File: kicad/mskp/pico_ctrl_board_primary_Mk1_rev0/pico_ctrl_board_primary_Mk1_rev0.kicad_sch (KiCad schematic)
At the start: 9 parts, among them J4 USB_C_Receptacle_USB2.0, J5 Conn_01x04_Socket, J8 Conn_01x12_Socket, J9 Conn_01x03_Socket, SW3 SW_Omron_B3FS, U1 Raspberry_Pi_Pico

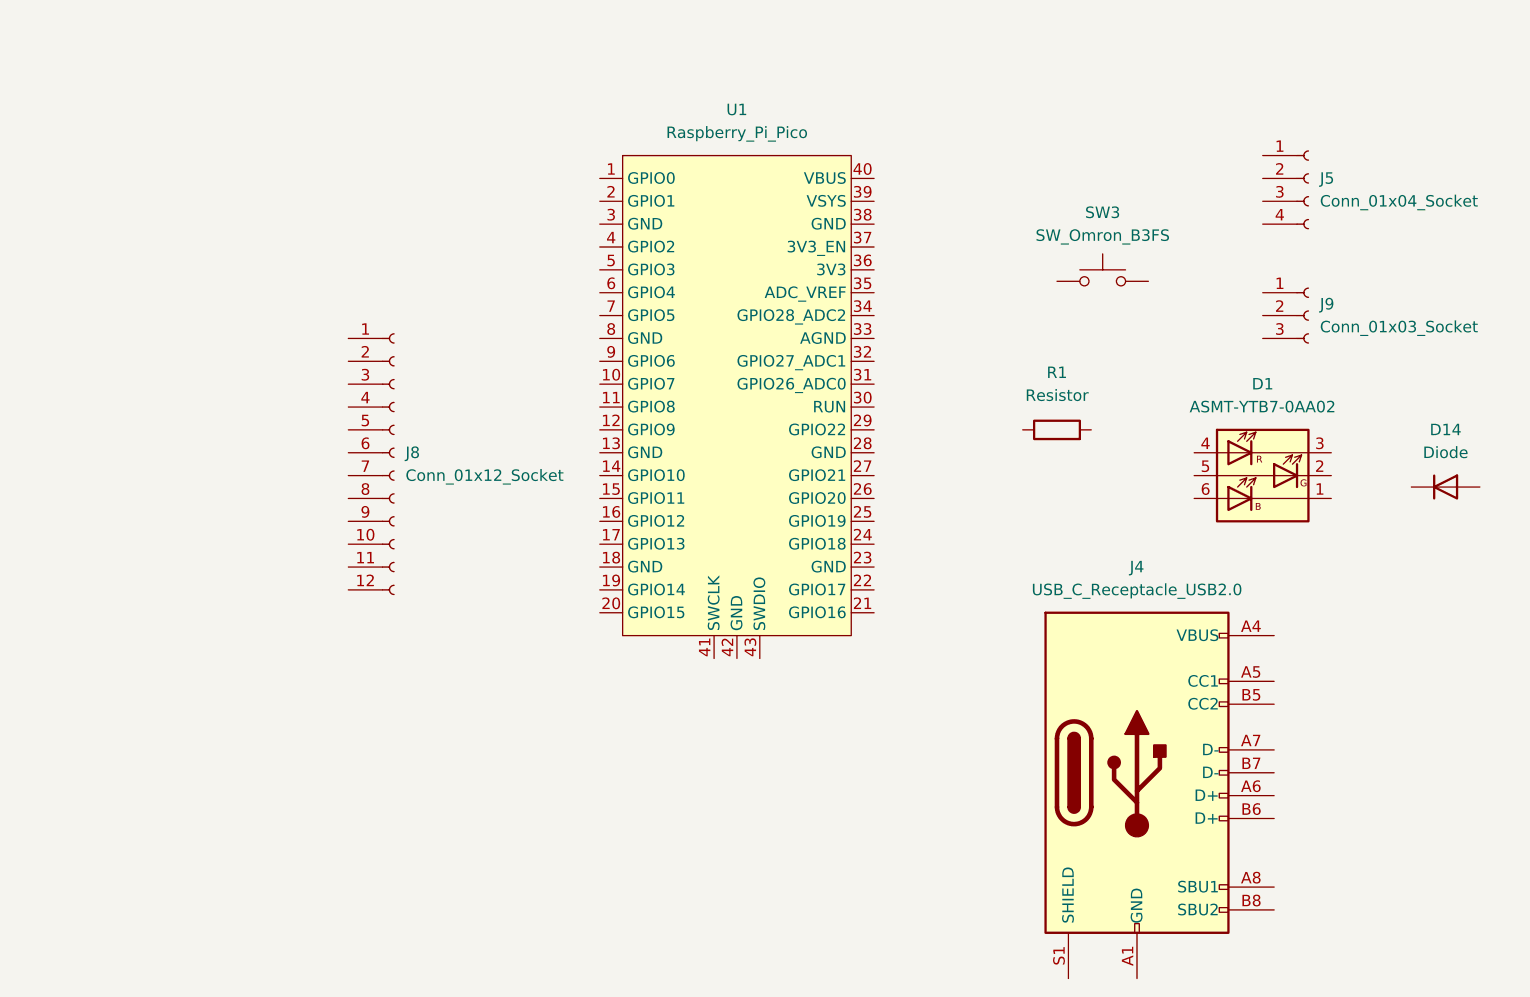
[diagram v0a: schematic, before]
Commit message: Removes the mksp_Mk1_rev0 project in favor of board-specific projects
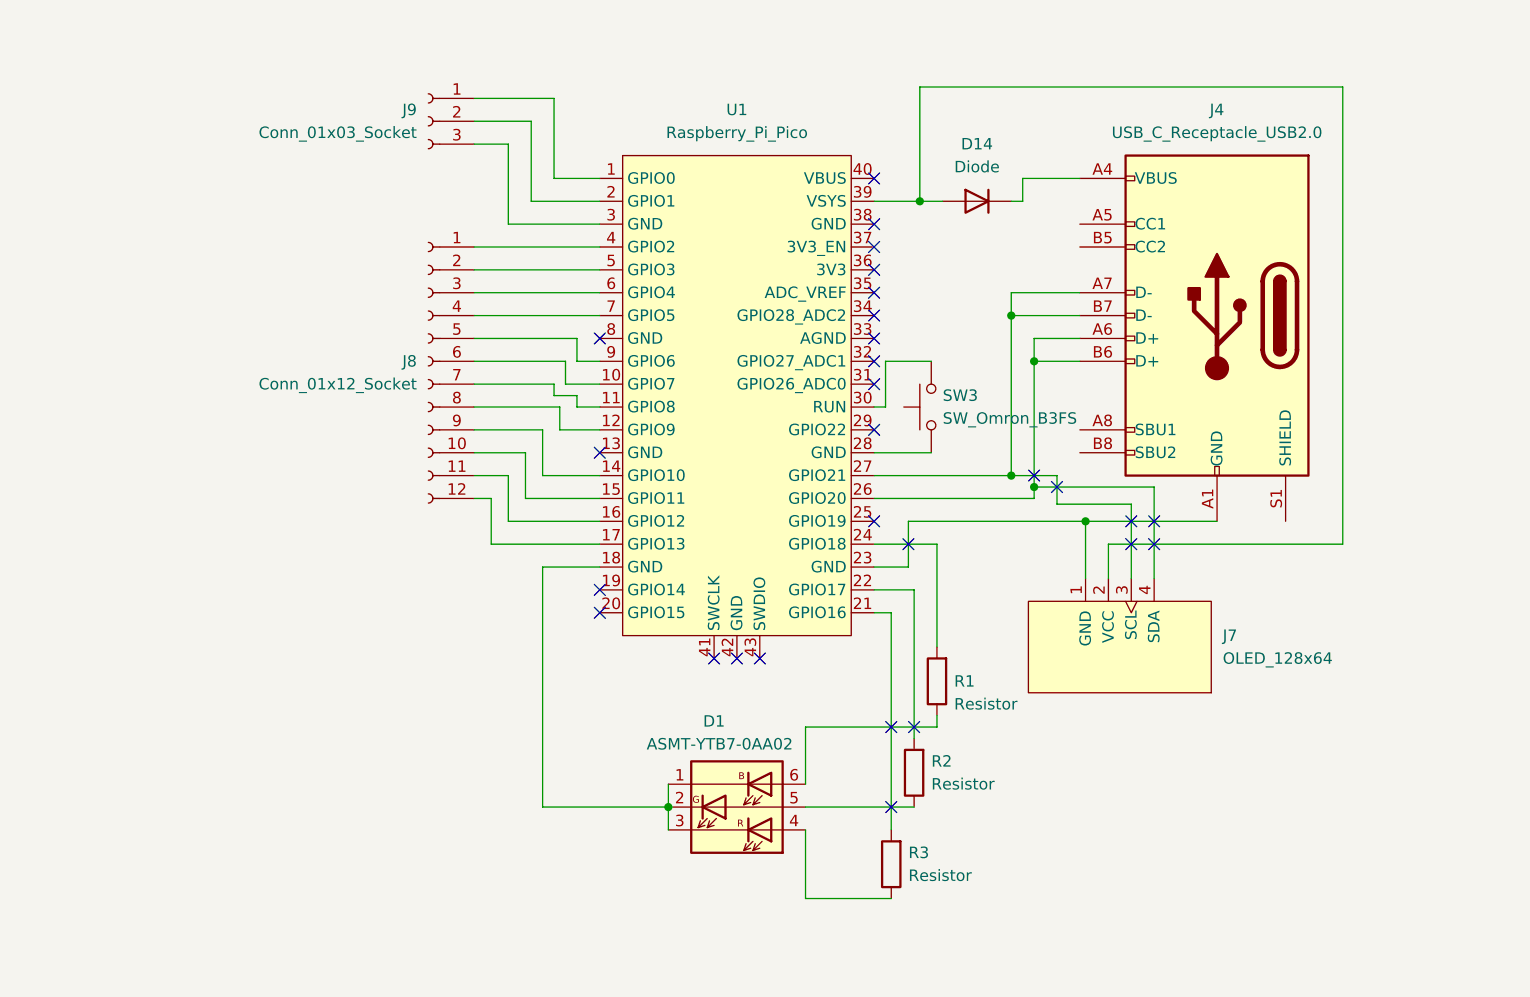
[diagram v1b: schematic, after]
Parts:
- removed J5: Conn_01x04_Socket, symbol Connector:Conn_01x04_Socket
- added J7: OLED_128x64, ScottoKeebs_Components:OLED_128x64, symbol ScottoKeebs:OLED_128x64
- added R2, R3: Resistor, symbol ScottoKeebs:Placeholder_Resistor
- D14: footprint (none) -> ScottoKeebs_Components:Diode_DO-35
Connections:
- net at U1.1 (GPIO0): now also J9.1 (Pin_1)
- net at U1.10 (GPIO7): now also J8.6 (Pin_6)
- net at U1.11 (GPIO8): now also J8.7 (Pin_7)
- net at U1.12 (GPIO9): now also J8.8 (Pin_8)
- net at U1.14 (GPIO10): now also J8.9 (Pin_9)
- net at U1.15 (GPIO11): now also J8.10 (Pin_10)
- net at U1.16 (GPIO12): now also J8.11 (Pin_11)
- net at U1.17 (GPIO13): now also J8.12 (Pin_12)
- net at U1.18 (GND): now also D1.1 (KB), D1.2 (KG), D1.3 (KR)
- net at U1.2 (GPIO1): now also J9.2 (Pin_2)
- net at U1.21 (GPIO16): now also R3.2
- net at U1.22 (GPIO17): now also R2.2
- net at U1.23 (GND): now also J4.A1 (GND), J4.A12 (GND), J4.B1 (GND), J4.B12 (GND), J7.1 (GND)
- net at U1.24 (GPIO18): now also R1.2
- net at U1.26 (GPIO20): now also J4.A6 (D+), J4.B6 (D+), J7.4 (SDA)
- net at U1.27 (GPIO21): now also J4.A7 (D-), J4.B7 (D-), J7.3 (SCL)
- net at U1.28 (GND): now also SW3.1
- net at U1.3 (GND): now also J9.3 (Pin_3)
- net at U1.30 (RUN): now also SW3.2
- net at U1.39 (VSYS): now also D14.2 (A), J7.2 (VCC)
- net at U1.4 (GPIO2): now also J8.1 (Pin_1)
- net at U1.5 (GPIO3): now also J8.2 (Pin_2)
- net at U1.6 (GPIO4): now also J8.3 (Pin_3)
- net at U1.7 (GPIO5): now also J8.4 (Pin_4)
- net at U1.9 (GPIO6): now also J8.5 (Pin_5)
- net at D14.1 (K): now also J4.A4 (VBUS), J4.A9 (VBUS), J4.B4 (VBUS), J4.B9 (VBUS)
- net at D1.4 (AR): now also R3.1
- net at D1.5 (AG): now also R2.1
- net at D1.6 (AB): now also R1.1
- no-connect marks 0 -> 28
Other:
- moved on the sheet: D1, D14, J4, J8, J9, R1, SW3

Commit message: Initial work on pico_ctrl_board_primary_Mk1_rev0 layout
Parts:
- added J1: Conn_01x06_Socket, symbol Connector:Conn_01x06_Socket
- J4: footprint (none) -> Connector_USB:USB_C_Receptacle_GCT_USB4110
- J8: footprint (none) -> Connector_JST:JST_GH_SM12B-GHS-TB_1x12-1MP_P1.25mm_Horizontal
- J9: footprint (none) -> Connector_JST:JST_SH_SM03B-SRSS-TB_1x03-1MP_P1.00mm_Horizontal
- R1, R2, R3: footprint (none) -> Resistor_THT:R_Axial_DIN0204_L3.6mm_D1.6mm_P5.08mm_Horizontal
- SW3: footprint (none) -> Button_Switch_SMD:SW_SPST_Omron_B3FS-101xP
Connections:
- net GND: now reaches U1.38 (GND)
- net +5V: now reaches U1.40 (VBUS)
- no-connect marks 28 -> 33
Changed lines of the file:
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@@
   (junction (at 151.13 123.19) (diameter 0) (color 0 0 0 0)
   )
-  (no_connect (at 173.99 58.42))
+  (no_connect (at 196.85 81.28))
   (no_connect (at 143.51 99.06))
   (no_connect (at 178.435 114.3))
@@
   (no_connect (at 173.99 63.5))
   (no_connect (at 175.895 114.3))
+  (no_connect (at 173.99 45.085))
   (no_connect (at 173.99 66.04))
+  (no_connect (at 196.85 83.82))
   (no_connect (at 173.99 76.2))
   (no_connect (at 143.51 71.12))
   (no_connect (at 177.8 93.98))
   (no_connect (at 202.565 93.98))
-  (no_connect (at 173.99 53.34))
   (no_connect (at 173.99 73.66))
   (no_connect (at 191.77 86.36))
@@
   (no_connect (at 173.99 68.58))
   (no_connect (at 175.895 123.19))
+  (no_connect (at 196.85 58.42))
   (no_connect (at 173.99 91.44))
   (no_connect (at 173.99 60.96))
   (no_connect (at 173.99 81.28))
+  (no_connect (at 196.85 60.96))
   (no_connect (at 202.565 91.44))
   (no_connect (at 143.51 101.6))
   (no_connect (at 161.29 106.68))
+  (no_connect (at 176.53 55.88))
+  (no_connect (at 219.71 91.44))
   (no_connect (at 205.105 93.98))
   (no_connect (at 173.99 71.12))
@@
     (stroke (width 0) (type default))
   )
+  (wire (pts (xy 168.275 41.275) (xy 168.275 45.085))
+    (stroke (width 0) (type default))
+  )
   (wire (pts (xy 143.51 76.2) (xy 139.7 76.2))
     (stroke (width 0) (type default))
@@
     (stroke (width 0) (type default))
   )
+  (wire (pts (xy 176.53 45.085) (xy 176.53 58.42))
+    (stroke (width 0) (type default))
+  )
   (wire (pts (xy 173.99 93.98) (xy 180.975 93.98))
     (stroke (width 0) (type default))
@@
     (stroke (width 0) (type default))
   )
+  (wire (pts (xy 168.275 45.085) (xy 176.53 45.085))
+    (stroke (width 0) (type default))
+  )
   (wire (pts (xy 173.99 99.06) (xy 178.435 99.06))
     (stroke (width 0) (type default))
@@
     (stroke (width 0) (type default))
   )
+  (wire (pts (xy 173.99 41.275) (xy 173.99 53.34))
+    (stroke (width 0) (type default))
+  )
   (wire (pts (xy 175.26 78.74) (xy 175.26 73.66))
+    (stroke (width 0) (type default))
+  )
+  (wire (pts (xy 176.53 58.42) (xy 173.99 58.42))
     (stroke (width 0) (type default))
   )
@@
         )
       )
+      (project "pico_ctrl_board_primary_Mk1_rev0"
+        (path "/cc93ba93-52c5-40e3-999d-01b7f0e97828"
+          (reference "U1") (unit 1)
+        )
+      )
     )
   )
@@
       (effects (font (size 1.27 1.27)) (justify right))
     )
-    (property "Footprint" "" (at 177.673 129.54 0)
+    (property "Footprint" "Resistor_THT:R_Axial_DIN0204_L3.6mm_D1.6mm_P5.08mm_Horizontal" (at 177.673 129.54 0)
       (effects (font (size 1.27 1.27)) hide)
     )
@@
         (path "/317db825-7ec8-42a4-86c9-29de77488848/9a4d8874-164c-4918-b768-ce32cb89a53f"
           (reference "R3") (unit 1)
+        )
+      )
+      (project "pico_ctrl_board_primary_Mk1_rev0"
+        (path "/cc93ba93-52c5-40e3-999d-01b7f0e97828"
+          (reference "R3") (unit 1)
+        )
+      )
+    )
+  )
+  (symbol (lib_id "power:GND") (at 168.275 41.275 180) (unit 1)
+    (in_bom yes) (on_board yes) (dnp no) (fields_autoplaced)
+    (property "Reference" "#PWR02" (at 168.275 34.925 0)
+      (effects (font (size 1.27 1.27)) hide)
+    )
+    (property "Value" "GND" (at 168.275 36.83 0)
+      (effects (font (size 1.27 1.27)))
+    )
+    (property "Footprint" "" (at 168.275 41.275 0)
+      (effects (font (size 1.27 1.27)) hide)
+    )
+    (property "Datasheet" "" (at 168.275 41.275 0)
+      (effects (font (size 1.27 1.27)) hide)
+    )
+    (pin "1")
+    (instances
+      (project "pico_ctrl_board_primary_Mk1_rev0"
+        (path "/cc93ba93-52c5-40e3-999d-01b7f0e97828"
+          (reference "#PWR02") (unit 1)
         )
       )
@@
       (project "mksp_Mk1_rev0"
         (path "/317db825-7ec8-42a4-86c9-29de77488848/9a4d8874-164c-4918-b768-ce32cb89a53f"
+          (reference "D14") (unit 1)
+        )
+      )
+      (project "pico_ctrl_board_primary_Mk1_rev0"
+        (path "/cc93ba93-52c5-40e3-999d-01b7f0e97828"
           (reference "D14") (unit 1)
         )
@@
       (effects (font (size 1.27 1.27)) (justify right))
     )
-    (property "Footprint" "" (at 175.26 78.74 0)
+    (property "Footprint" "Button_Switch_SMD:SW_SPST_Omron_B3FS-101xP" (at 175.26 78.74 0)
       (effects (font (size 1.27 1.27)) hide)
     )
@@
       (project "mksp_Mk1_rev0"
         (path "/317db825-7ec8-42a4-86c9-29de77488848/9a4d8874-164c-4918-b768-ce32cb89a53f"
+          (reference "SW3") (unit 1)
+        )
+      )
+      (project "pico_ctrl_board_primary_Mk1_rev0"
+        (path "/cc93ba93-52c5-40e3-999d-01b7f0e97828"
           (reference "SW3") (unit 1)
         )
@@
       (effects (font (size 1.27 1.27)) (justify right))
     )
-    (property "Footprint" "" (at 180.213 119.38 0)
+    (property "Footprint" "Resistor_THT:R_Axial_DIN0204_L3.6mm_D1.6mm_P5.08mm_Horizontal" (at 180.213 119.38 0)
       (effects (font (size 1.27 1.27)) hide)
     )
@@
       (project "mksp_Mk1_rev0"
         (path "/317db825-7ec8-42a4-86c9-29de77488848/9a4d8874-164c-4918-b768-ce32cb89a53f"
+          (reference "R2") (unit 1)
+        )
+      )
+      (project "pico_ctrl_board_primary_Mk1_rev0"
+        (path "/cc93ba93-52c5-40e3-999d-01b7f0e97828"
           (reference "R2") (unit 1)
         )
@@
       (effects (font (size 1.27 1.27)) (justify left))
     )
-    (property "Footprint" "" (at 124.46 73.66 0)
+    (property "Footprint" "Connector_JST:JST_GH_SM12B-GHS-TB_1x12-1MP_P1.25mm_Horizontal" (at 124.46 73.66 0)
       (effects (font (size 1.27 1.27)) hide)
     )
@@
         )
       )
+      (project "pico_ctrl_board_primary_Mk1_rev0"
+        (path "/cc93ba93-52c5-40e3-999d-01b7f0e97828"
+          (reference "J8") (unit 1)
+        )
+      )
     )
   )
@@
       (effects (font (size 1.27 1.27)))
     )
-    (property "Footprint" "" (at 208.28 68.58 0)
+    (property "Footprint" "Connector_USB:USB_C_Receptacle_GCT_USB4110" (at 208.28 68.58 0)
       (effects (font (size 1.27 1.27)) hide)
     )
@@
         )
       )
+      (project "pico_ctrl_board_primary_Mk1_rev0"
+        (path "/cc93ba93-52c5-40e3-999d-01b7f0e97828"
+          (reference "J4") (unit 1)
+        )
+      )
+    )
+  )
+  (symbol (lib_id "Connector:Conn_01x06_Socket") (at 88.9 64.135 180) (unit 1)
+    (in_bom yes) (on_board yes) (dnp no) (fields_autoplaced)
+    (property "Reference" "J1" (at 89.535 51.435 0)
+      (effects (font (size 1.27 1.27)))
+    )
+    (property "Value" "Conn_01x06_Socket" (at 89.535 53.975 0)
+      (effects (font (size 1.27 1.27)))
+    )
+    (property "Footprint" "" (at 88.9 64.135 0)
+      (effects (font (size 1.27 1.27)) hide)
+    )
+    (property "Datasheet" "~" (at 88.9 64.135 0)
+      (effects (font (size 1.27 1.27)) hide)
+    )
+    (pin "1")
+    (pin "2")
+    (pin "3")
+    (pin "4")
+    (pin "5")
+    (pin "6")
+    (instances
+      (project "pico_ctrl_board_primary_Mk1_rev0"
+        (path "/cc93ba93-52c5-40e3-999d-01b7f0e97828"
+          (reference "J1") (unit 1)
+        )
+      )
     )
   )
@@
       (effects (font (size 1.27 1.27)) (justify left))
     )
-    (property "Footprint" "" (at 124.46 46.99 0)
+    (property "Footprint" "Connector_JST:JST_SH_SM03B-SRSS-TB_1x03-1MP_P1.00mm_Horizontal" (at 124.46 46.99 0)
       (effects (font (size 1.27 1.27)) hide)
     )
@@
         (path "/317db825-7ec8-42a4-86c9-29de77488848/9a4d8874-164c-4918-b768-ce32cb89a53f"
           (reference "J9") (unit 1)
+        )
+      )
+      (project "pico_ctrl_board_primary_Mk1_rev0"
+        (path "/cc93ba93-52c5-40e3-999d-01b7f0e97828"
+          (reference "J9") (unit 1)
+        )
+      )
+    )
+  )
+  (symbol (lib_id "power:+5V") (at 173.99 41.275 0) (unit 1)
+    (in_bom yes) (on_board yes) (dnp no) (fields_autoplaced)
+    (property "Reference" "#PWR01" (at 173.99 45.085 0)
+      (effects (font (size 1.27 1.27)) hide)
+    )
+    (property "Value" "+5V" (at 173.99 36.83 0)
+      (effects (font (size 1.27 1.27)))
+    )
+    (property "Footprint" "" (at 173.99 41.275 0)
+      (effects (font (size 1.27 1.27)) hide)
+    )
+    (property "Datasheet" "" (at 173.99 41.275 0)
+      (effects (font (size 1.27 1.27)) hide)
+    )
+    (pin "1")
+    (instances
+      (project "pico_ctrl_board_primary_Mk1_rev0"
+        (path "/cc93ba93-52c5-40e3-999d-01b7f0e97828"
+          (reference "#PWR01") (unit 1)
         )
       )
@@
         )
       )
+      (project "pico_ctrl_board_primary_Mk1_rev0"
+        (path "/cc93ba93-52c5-40e3-999d-01b7f0e97828"
+          (reference "J7") (unit 1)
+        )
+      )
     )
   )
@@
         )
       )
+      (project "pico_ctrl_board_primary_Mk1_rev0"
+        (path "/cc93ba93-52c5-40e3-999d-01b7f0e97828"
+          (reference "D1") (unit 1)
+        )
+      )
     )
   )
@@
       (effects (font (size 1.27 1.27)) (justify right))
     )
-    (property "Footprint" "" (at 182.753 109.22 0)
+    (property "Footprint" "Resistor_THT:R_Axial_DIN0204_L3.6mm_D1.6mm_P5.08mm_Horizontal" (at 182.753 109.22 0)
       (effects (font (size 1.27 1.27)) hide)
     )
@@
         )
       )
-    )
+      (project "pico_ctrl_board_primary_Mk1_rev0"
+        (path "/cc93ba93-52c5-40e3-999d-01b7f0e97828"
+          (reference "R1") (unit 1)
+        )
+      )
+    )
+  )
+  (sheet_instances
+    (path "/" (page "1"))
   )
 )
